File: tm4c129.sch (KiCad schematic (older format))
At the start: 14 parts, among them U1 TM4C1294NCPDTGOOD, Y1 Crystal_GND24

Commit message: added some more stuff
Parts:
- Y1: footprint Crystals:Crystal_SMD_3225-4pin_3.2x2.5mm -> Crystal:Crystal_SMD_3225-4Pin_3.2x2.5mm
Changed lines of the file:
@@
 $Descr A4 11693 8268
 encoding utf-8
-Sheet 2 3
+Sheet 2 4
 Title ""
 Date ""
@@
 F 0 "Y1" V 3004 4441 50  0000 L CNN
 F 1 "Crystal_GND24" V 3450 4200 50  0000 L CNN
-F 2 "Crystals:Crystal_SMD_3225-4pin_3.2x2.5mm" H 3050 4200 50  0001 C CNN
+F 2 "Crystal:Crystal_SMD_3225-4Pin_3.2x2.5mm" H 3050 4200 50  0001 C CNN
 F 3 "~" H 3050 4200 50  0001 C CNN
 	1    3050 4200

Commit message: layout stuff
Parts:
- U1: symbol WRaptor1201-A-eagle-import:TM4C1294NCPDTGOOD -> Exodus_Microcontrollers:TM4C1294NCPDTGOOD-WRaptor1201-A-eagle-import
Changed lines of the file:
@@
 	2950 4000 3050 4000
 $Comp
-L WRaptor1201-A-eagle-import:TM4C1294NCPDTGOOD U1
+L Exodus_Microcontrollers:TM4C1294NCPDTGOOD-WRaptor1201-A-eagle-import U1
 U 1 1 5C7FA546
 P 5450 4150
+AR Path="/5C7FA546" Ref="U1"  Part="1"
+AR Path="/5C80AE96/5C7FA546" Ref="U1"  Part="1"
 F 0 "U1" H 5450 7536 59  0000 C CNN
 F 1 "TM4C1294NCPDTGOOD" H 5450 7431 59  0000 C CNN

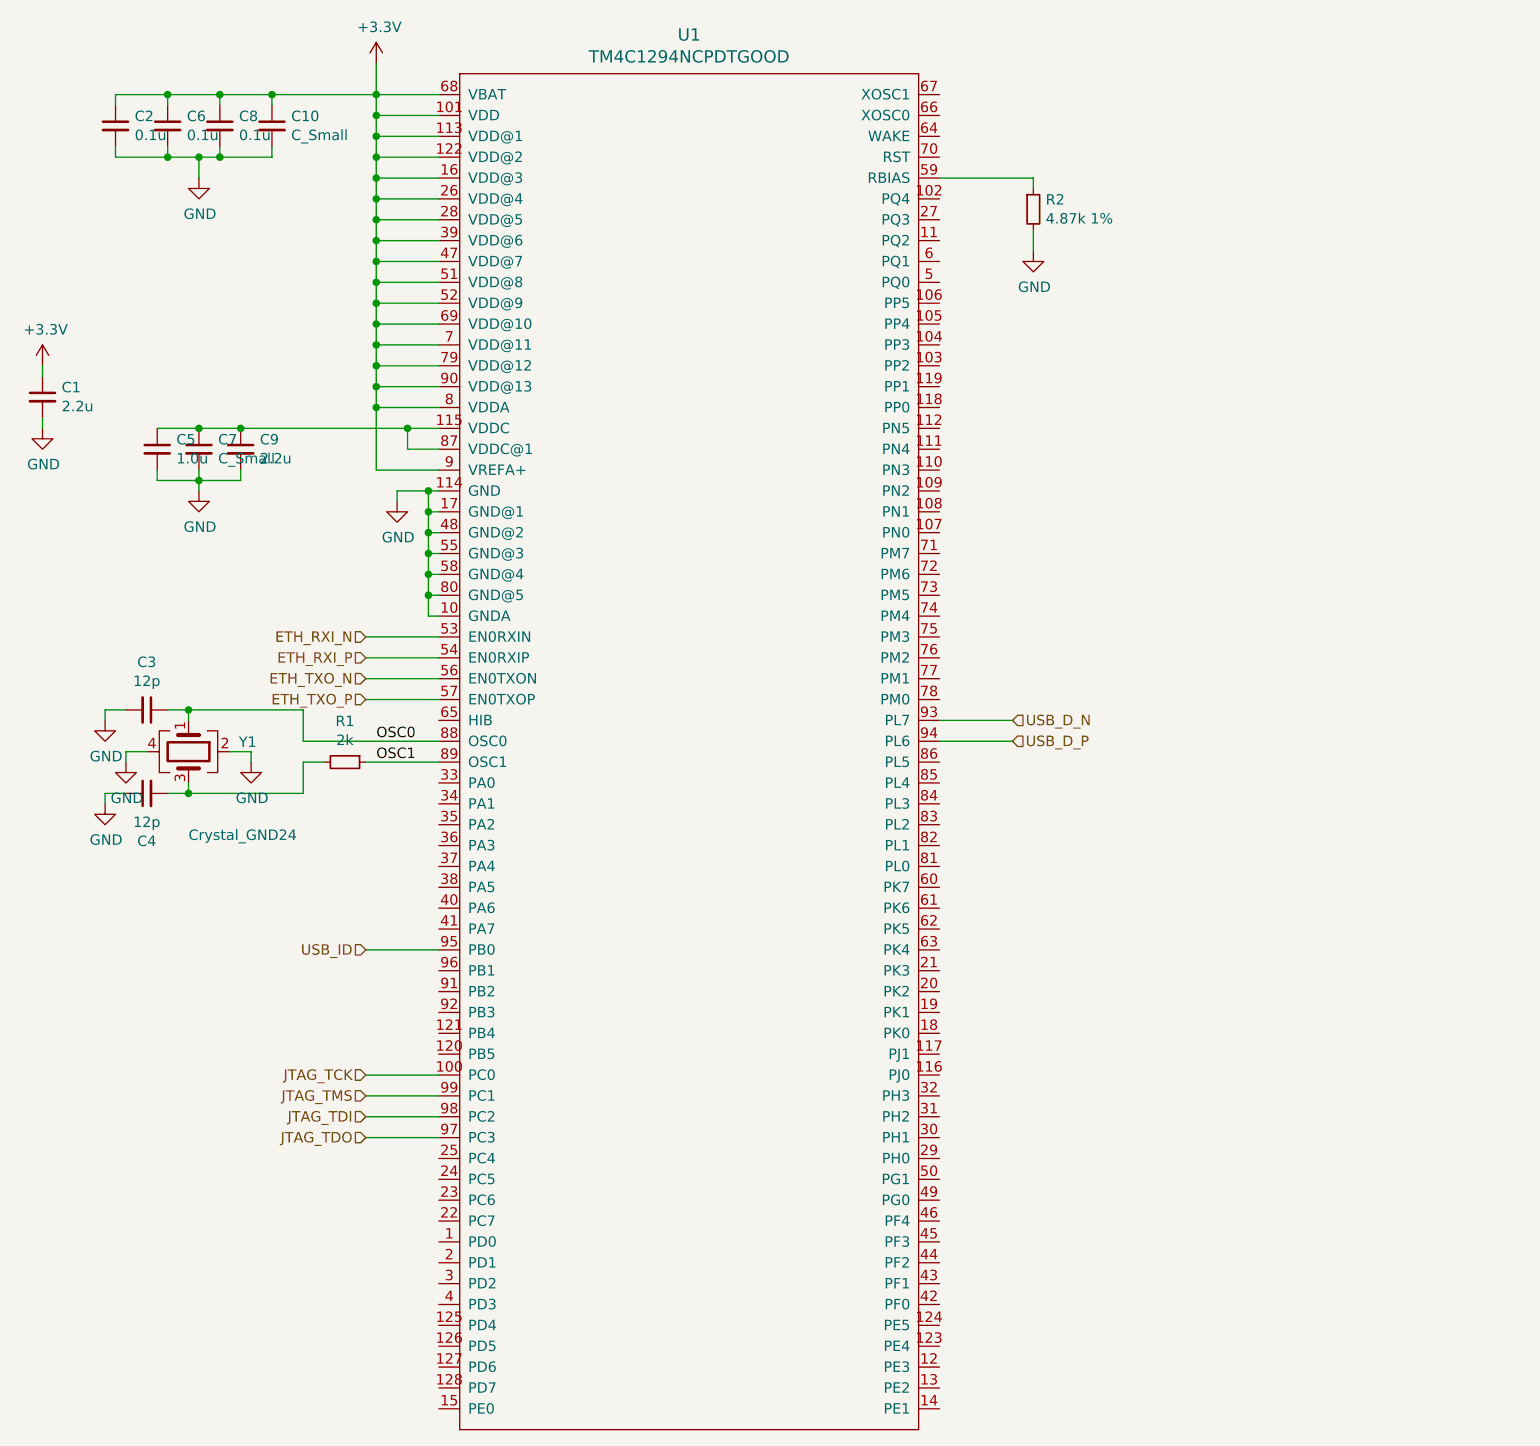
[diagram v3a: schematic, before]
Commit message: schematics for expansion slots and memory
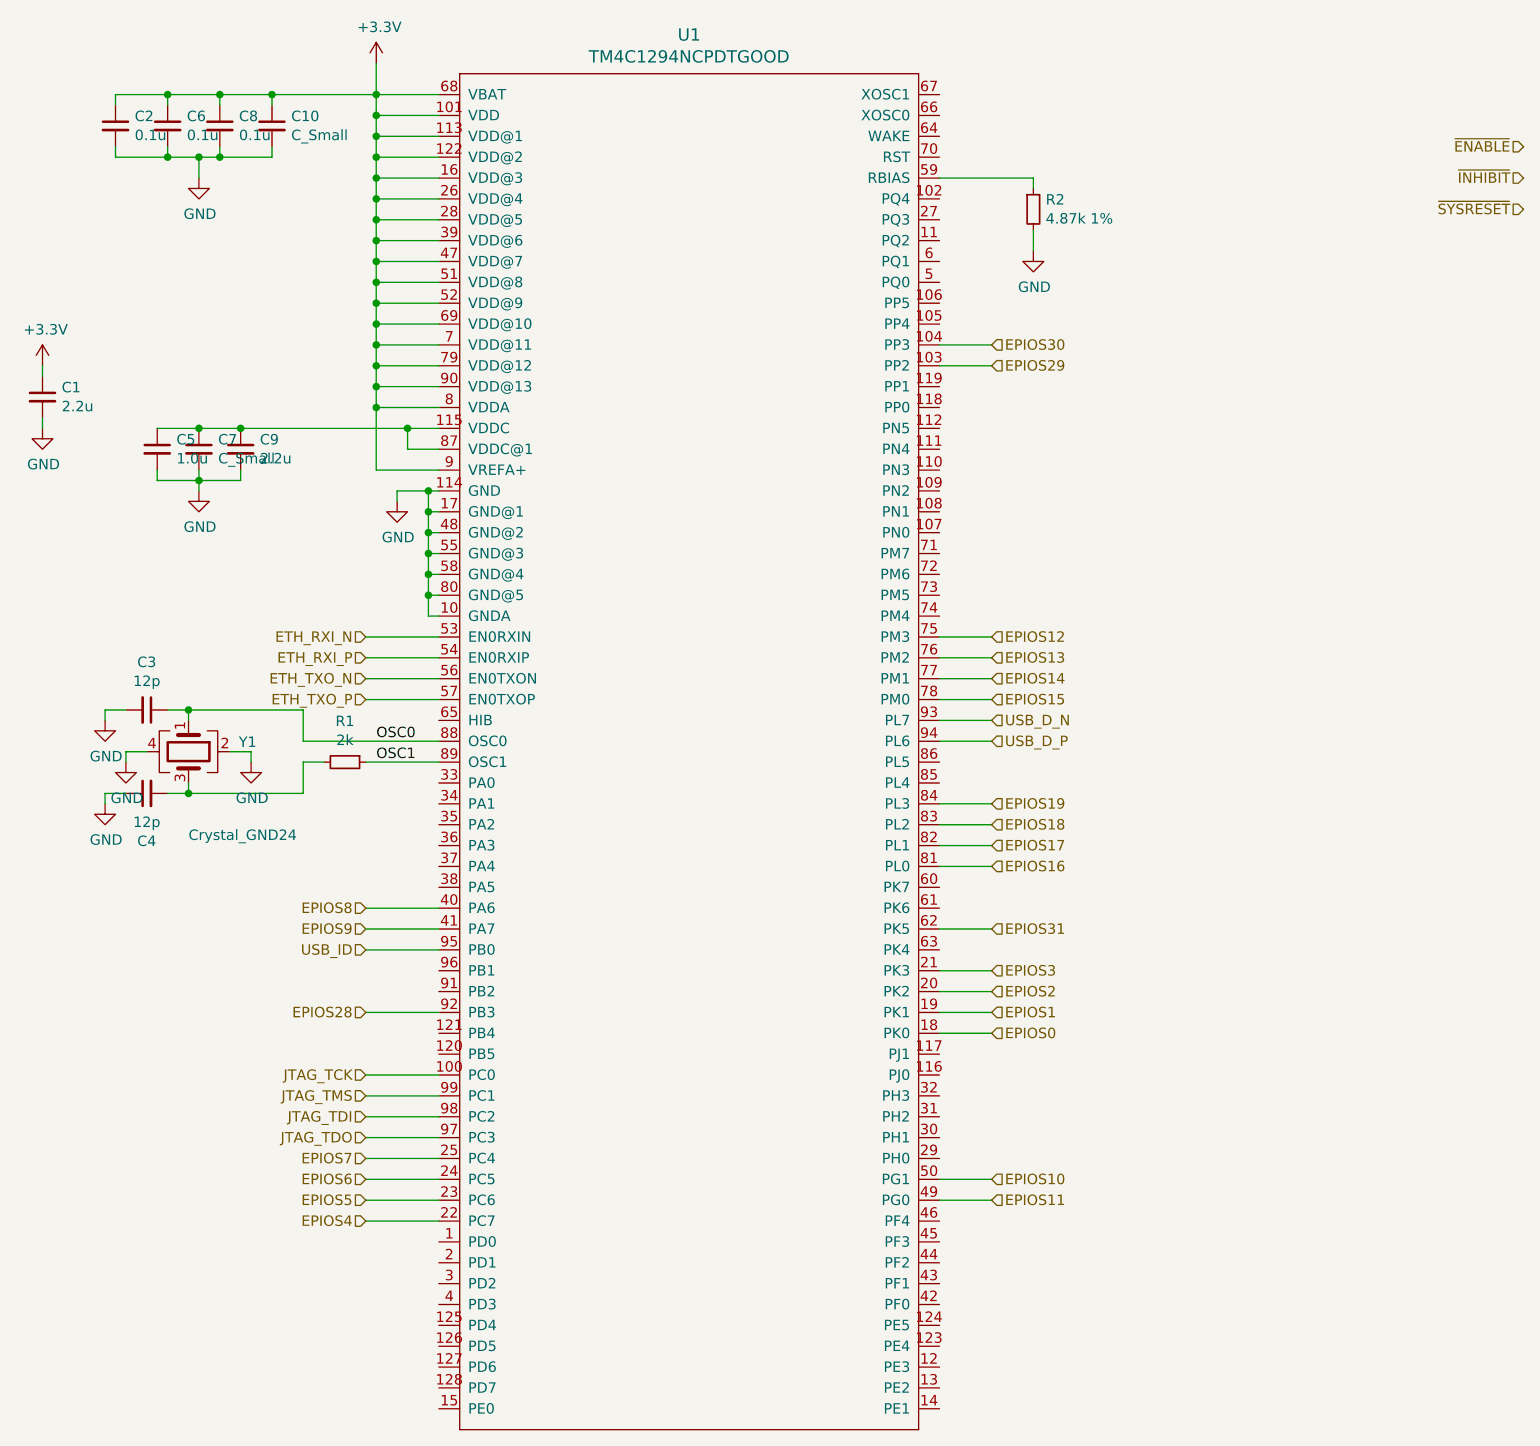
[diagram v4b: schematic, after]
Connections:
- net EPIOS29: now reaches U1.103 (PP2)
- net EPIOS30: now reaches U1.104 (PP3)
- net EPIOS0: now reaches U1.18 (PK0)
- net EPIOS1: now reaches U1.19 (PK1)
- net EPIOS2: now reaches U1.20 (PK2)
- net EPIOS3: now reaches U1.21 (PK3)
- net EPIOS4: now reaches U1.22 (PC7)
- net EPIOS5: now reaches U1.23 (PC6)
- net EPIOS6: now reaches U1.24 (PC5)
- net EPIOS7: now reaches U1.25 (PC4)
- net EPIOS8: now reaches U1.40 (PA6)
- net EPIOS9: now reaches U1.41 (PA7)
- net EPIOS11: now reaches U1.49 (PG0)
- net EPIOS10: now reaches U1.50 (PG1)
- net EPIOS31: now reaches U1.62 (PK5)
- net EPIOS12: now reaches U1.75 (PM3)
- net EPIOS13: now reaches U1.76 (PM2)
- net EPIOS14: now reaches U1.77 (PM1)
- net EPIOS15: now reaches U1.78 (PM0)
- net EPIOS16: now reaches U1.81 (PL0)
- net EPIOS17: now reaches U1.82 (PL1)
- net EPIOS18: now reaches U1.83 (PL2)
- net EPIOS19: now reaches U1.84 (PL3)
- net EPIOS28: now reaches U1.92 (PB3)
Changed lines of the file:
@@
 $Descr A4 11693 8268
 encoding utf-8
-Sheet 2 5
+Sheet 2 10
 Title ""
 Date "2019-03-16"
@@
 JTAG_TDO
 Wire Wire Line
-	6650 4050 7000 4050
-Wire Wire Line
-	6650 4150 7000 4150
-Text HLabel 7000 4050 2    50   Input ~ 0
+	6650 4050 6900 4050
+Wire Wire Line
+	6650 4150 6900 4150
+Text HLabel 6900 4050 2    50   Input ~ 0
 USB_D_N
-Text HLabel 7000 4150 2    50   Input ~ 0
+Text HLabel 6900 4150 2    50   Input ~ 0
 USB_D_P
 Wire Wire Line
@@
 Wire Wire Line
 	2350 2650 2350 2600
+Text HLabel 6900 5550 2    50   Input ~ 0
+EPIOS0
+Text HLabel 6900 5450 2    50   Input ~ 0
+EPIOS1
+Text HLabel 6900 5350 2    50   Input ~ 0
+EPIOS2
+Text HLabel 6900 5250 2    50   Input ~ 0
+EPIOS3
+Text HLabel 3900 6450 0    50   Input ~ 0
+EPIOS4
+Text HLabel 3900 6350 0    50   Input ~ 0
+EPIOS5
+Text HLabel 3900 6250 0    50   Input ~ 0
+EPIOS6
+Text HLabel 3900 6150 0    50   Input ~ 0
+EPIOS7
+Text HLabel 3900 4950 0    50   Input ~ 0
+EPIOS8
+Text HLabel 3900 5050 0    50   Input ~ 0
+EPIOS9
+Text HLabel 6900 6250 2    50   Input ~ 0
+EPIOS10
+Text HLabel 6900 6350 2    50   Input ~ 0
+EPIOS11
+Text HLabel 6900 3650 2    50   Input ~ 0
+EPIOS12
+Text HLabel 6900 3750 2    50   Input ~ 0
+EPIOS13
+Text HLabel 6900 3850 2    50   Input ~ 0
+EPIOS14
+Text HLabel 6900 3950 2    50   Input ~ 0
+EPIOS15
+Text HLabel 6900 4750 2    50   Input ~ 0
+EPIOS16
+Text HLabel 6900 4650 2    50   Input ~ 0
+EPIOS17
+Text HLabel 6900 4550 2    50   Input ~ 0
+EPIOS18
+Text HLabel 6900 4450 2    50   Input ~ 0
+EPIOS19
+Wire Wire Line
+	6900 5550 6650 5550
+Wire Wire Line
+	6900 5450 6650 5450
+Wire Wire Line
+	6900 5350 6650 5350
+Wire Wire Line
+	6900 5250 6650 5250
+Wire Wire Line
+	3900 6450 4250 6450
+Wire Wire Line
+	6900 6250 6650 6250
+Wire Wire Line
+	6900 6350 6650 6350
+Wire Wire Line
+	6900 3650 6650 3650
+Wire Wire Line
+	6900 3750 6650 3750
+Wire Wire Line
+	6900 3850 6650 3850
+Wire Wire Line
+	6900 3950 6650 3950
+Wire Wire Line
+	6900 4750 6650 4750
+Wire Wire Line
+	6900 4650 6650 4650
+Wire Wire Line
+	6900 4550 6650 4550
+Wire Wire Line
+	6900 4450 6650 4450
+Text HLabel 3900 5450 0    50   Input ~ 0
+EPIOS28
+Wire Wire Line
+	3900 5450 4250 5450
+Text HLabel 6900 2350 2    50   Input ~ 0
+EPIOS29
+Wire Wire Line
+	6900 2350 6650 2350
+Text HLabel 6900 2250 2    50   Input ~ 0
+EPIOS30
+Wire Wire Line
+	6900 2250 6650 2250
+Text HLabel 6900 5050 2    50   Input ~ 0
+EPIOS31
+Wire Wire Line
+	6900 5050 6650 5050
+Wire Wire Line
+	3900 6350 4250 6350
+Wire Wire Line
+	3900 6250 4250 6250
+Wire Wire Line
+	3900 6150 4250 6150
+Wire Wire Line
+	3900 4950 4250 4950
+Wire Wire Line
+	3900 5050 4250 5050
+Text HLabel 9450 1300 0    50   Input ~ 0
+~ENABLE
+Text HLabel 9450 1450 0    50   Input ~ 0
+~INHIBIT
+Text HLabel 9450 1600 0    50   Input ~ 0
+~SYSRESET
 $EndSCHEMATC

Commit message: layout done sans connector. It's pretty big. Likely going to need to tear some of this up.
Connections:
- net SPI_MISO: now reaches U1.1 (PD0)
- net SPI_DAT3: now reaches U1.127 (PD6)
- net SPI_DAT2: now reaches U1.128 (PD7)
- net SPI_MOSI: now reaches U1.2 (PD1)
- net SPI_SS: now reaches U1.3 (PD2)
- net SPI_SCLK: now reaches U1.4 (PD3)
- net ETH_LED0: now reaches U1.42 (PF0)
- net ETH_LED1: now reaches U1.46 (PF4)
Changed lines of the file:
@@
 Text HLabel 9450 1600 0    50   Input ~ 0
 ~SYSRESET
+Wire Wire Line
+	4250 6650 3900 6650
+Wire Wire Line
+	4250 6750 3900 6750
+Wire Wire Line
+	4250 6850 3900 6850
+Wire Wire Line
+	4250 6550 3900 6550
+Text HLabel 3900 6550 0    50   Input ~ 0
+SPI_MISO
+Text HLabel 3900 6650 0    50   Input ~ 0
+SPI_MOSI
+Text HLabel 3900 6750 0    50   Input ~ 0
+SPI_SS
+Text HLabel 3900 6850 0    50   Input ~ 0
+SPI_SCLK
+Wire Wire Line
+	4250 7150 3900 7150
+Wire Wire Line
+	4250 7250 3900 7250
+Text HLabel 3900 7150 0    50   Input ~ 0
+SPI_DAT3
+Text HLabel 3900 7250 0    50   Input ~ 0
+SPI_DAT2
+Wire Wire Line
+	6650 6450 6900 6450
+Wire Wire Line
+	6650 6850 6900 6850
+Text HLabel 6900 6850 2    50   Input ~ 0
+ETH_LED0
+Text HLabel 6900 6450 2    50   Input ~ 0
+ETH_LED1
 $EndSCHEMATC
